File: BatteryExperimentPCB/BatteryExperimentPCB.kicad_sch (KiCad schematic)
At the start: 32 parts, among them J1 USB_C_Receptacle_USB2.0_14P, J2 Conn_01x11_Pin, J3 Conn_01x11_Pin, Q1 DMG1012T, SW1 SW_Push, U1 ATtiny3226-M, U2 USBLC6-2P6, U3 BQ25628RYKR

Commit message: cleanup
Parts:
- D2: footprint (none) -> LED_SMD:LED_0805_2012Metric
- L1: footprint (none) -> Inductor_SMD:L_0805_2012Metric
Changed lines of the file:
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@@
 			)
 		)
-		(property "Footprint" ""
+		(property "Footprint" "Inductor_SMD:L_0805_2012Metric"
 			(at 168.91 55.88 0)
 			(effects
@@
 			)
 		)
-		(property "Footprint" ""
+		(property "Footprint" "LED_SMD:LED_0805_2012Metric"
 			(at 207.01 72.39 0)
 			(effects

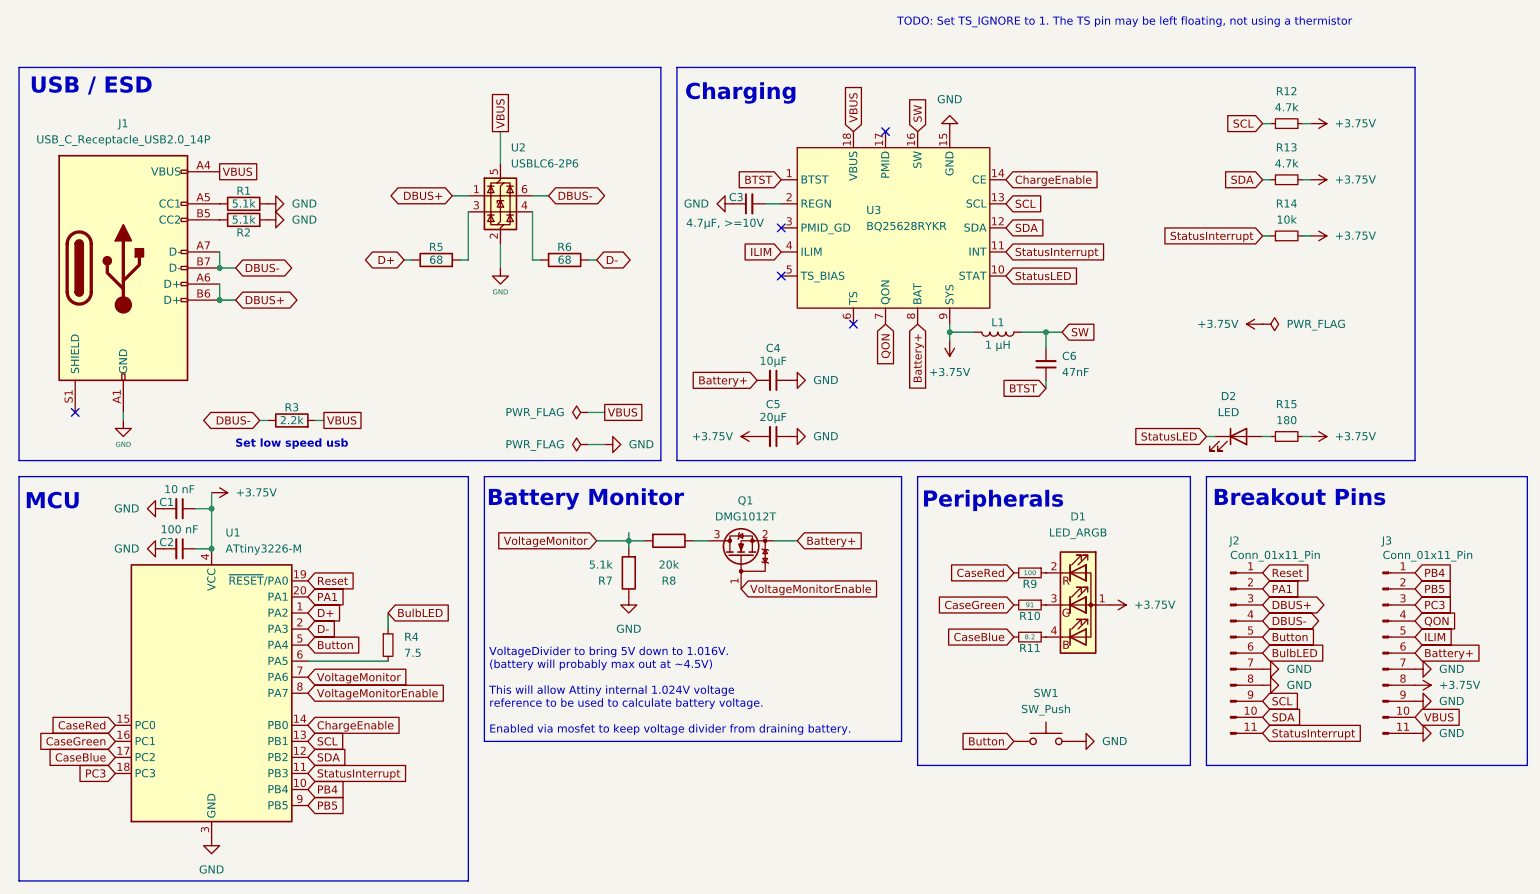
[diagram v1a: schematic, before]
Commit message: add PMID and PMID_GO pins to breakout
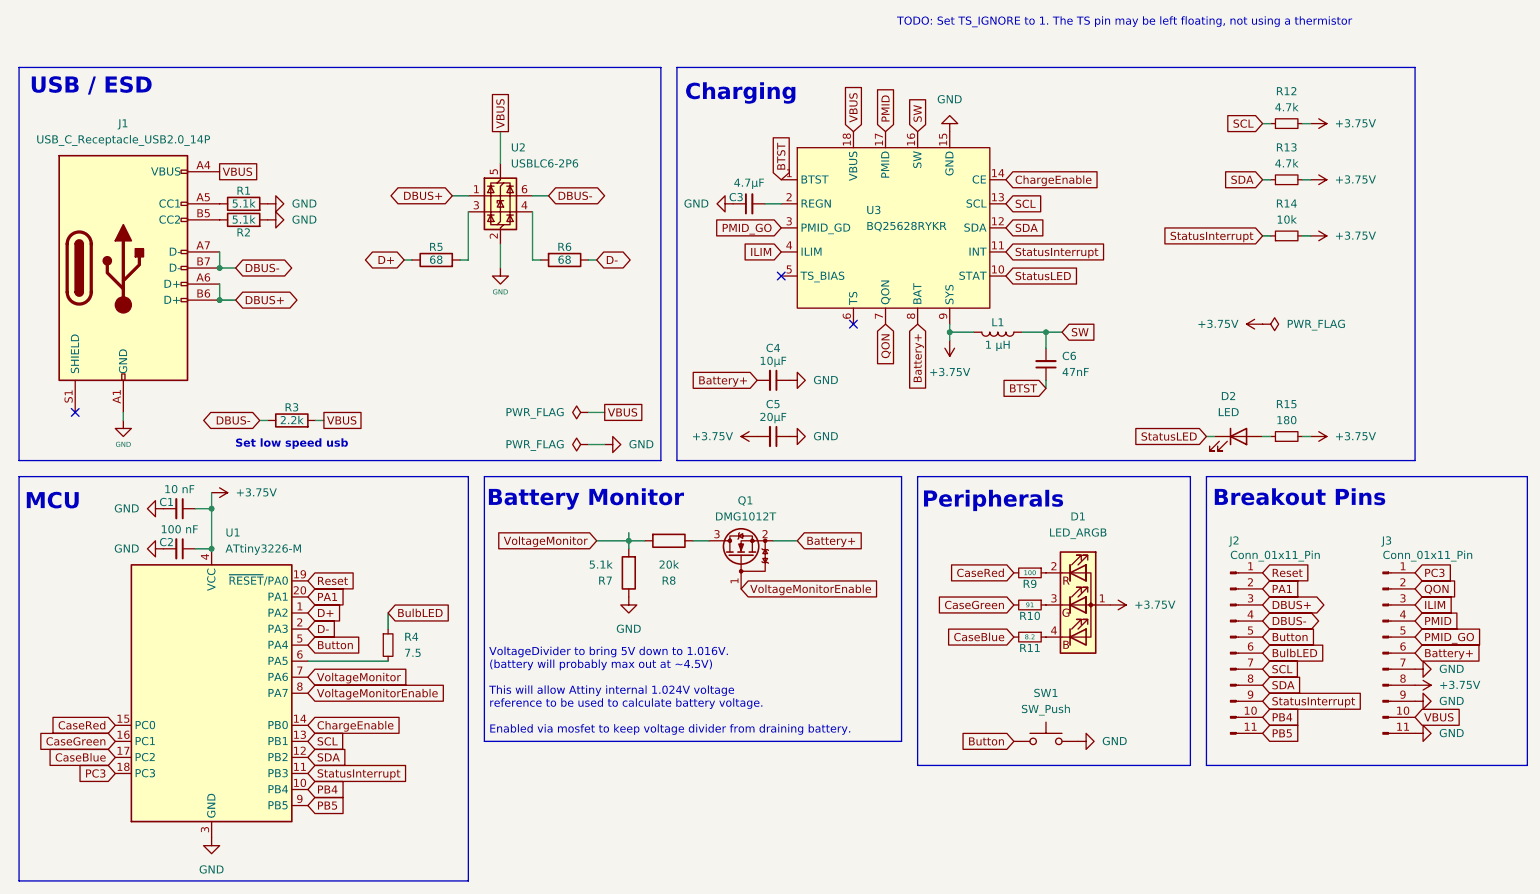
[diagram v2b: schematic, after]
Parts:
- C3: value 4.7μF, >=10V -> 4.7μF
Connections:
- net GND: no longer J2.7 (Pin_7), J2.8 (Pin_8)
- net ILIM: now also J3.3 (Pin_3); no longer J3.5 (Pin_5)
- net PB4: now also J2.10 (Pin_10); no longer J3.1 (Pin_1)
- net PB5: now also J2.11 (Pin_11); no longer J3.2 (Pin_2)
- net PC3: now also J3.1 (Pin_1); no longer J3.3 (Pin_3)
- net QON: now also J3.2 (Pin_2); no longer J3.4 (Pin_4)
- net SCL: now also J2.7 (Pin_7); no longer J2.9 (Pin_9)
- net SDA: now also J2.8 (Pin_8); no longer J2.10 (Pin_10)
- net StatusInterrupt: now also J2.9 (Pin_9); no longer J2.11 (Pin_11)
- net PMID: now reaches U3.17 (PMID)
- net PMID: now also J3.4 (Pin_4)
- net PMID_GO: now reaches U3.3 (PMID_GD)
- net PMID_GO: now also J3.5 (Pin_5)
- no-connect marks 5 -> 3

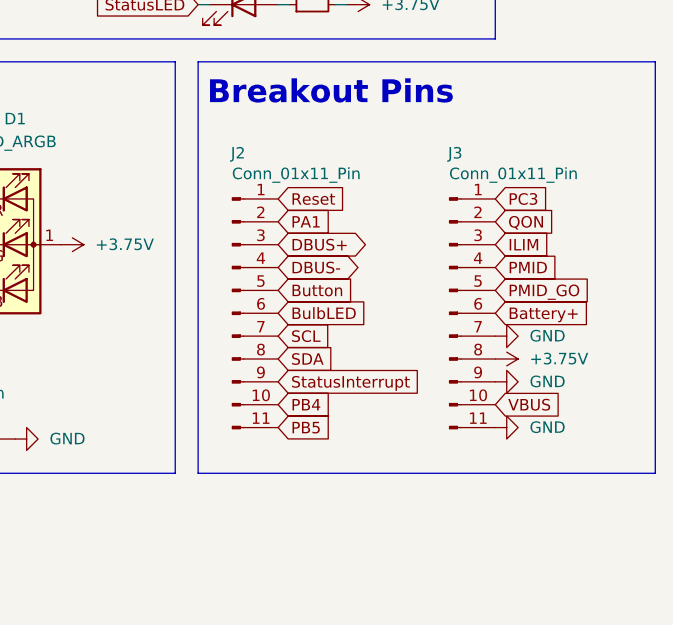
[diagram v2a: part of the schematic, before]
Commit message: added 12th row to breakout, cleanup
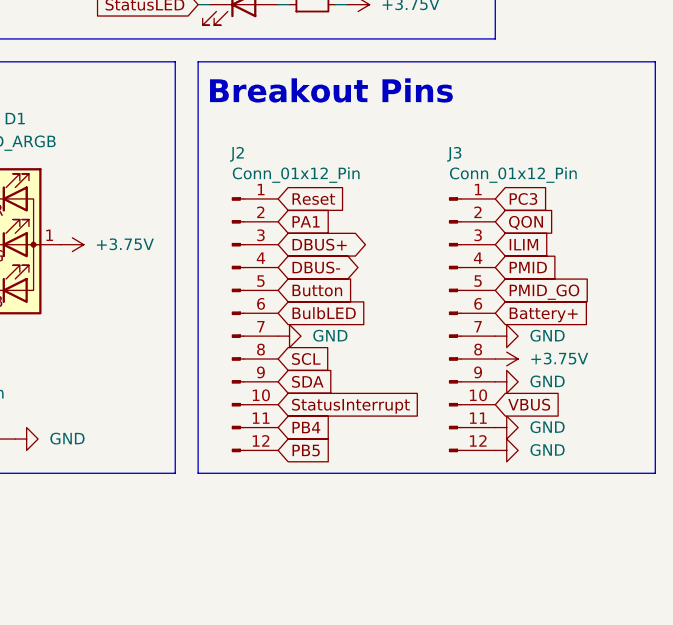
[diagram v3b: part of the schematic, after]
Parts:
- removed J2, J3: Conn_01x11_Pin, Connector_PinHeader_2.54mm:PinHeader_1x11_P2.54mm_Vertical, symbol Connector:Conn_01x11_Pin
- added J2, J3: Conn_01x12_Pin, symbol Connector:Conn_01x12_Pin
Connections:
- net +3.75V: now also J3.8 (Pin_8)
- net Battery+: now also J3.6 (Pin_6)
- net BulbLED: now also J2.6 (Pin_6)
- net Button: now also J2.5 (Pin_5)
- net DBUS+: now also J2.3 (Pin_3)
- net DBUS-: now also J2.4 (Pin_4)
- net GND: now also J2.7 (Pin_7), J3.11 (Pin_11), J3.12 (Pin_12), J3.7 (Pin_7), J3.9 (Pin_9)
- net ILIM: now also J3.3 (Pin_3)
- net PA1: now also J2.2 (Pin_2)
- net PB4: now also J2.11 (Pin_11)
- net PB5: now also J2.12 (Pin_12)
- net PC3: now also J3.1 (Pin_1)
- net PMID: now also J3.4 (Pin_4)
- net PMID_GO: now also J3.5 (Pin_5)
- net QON: now also J3.2 (Pin_2)
- net Reset: now also J2.1 (Pin_1)
- net SCL: now also J2.8 (Pin_8)
- net SDA: now also J2.9 (Pin_9)
- net StatusInterrupt: now also J2.10 (Pin_10)
- net VBUS: now also J3.10 (Pin_10)

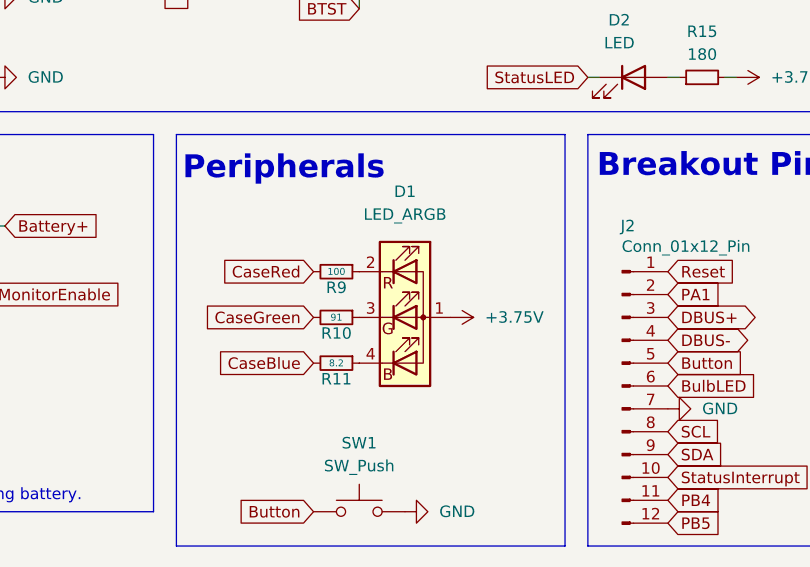
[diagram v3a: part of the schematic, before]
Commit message: copied and customised LED_RBGA symbol for chosen part
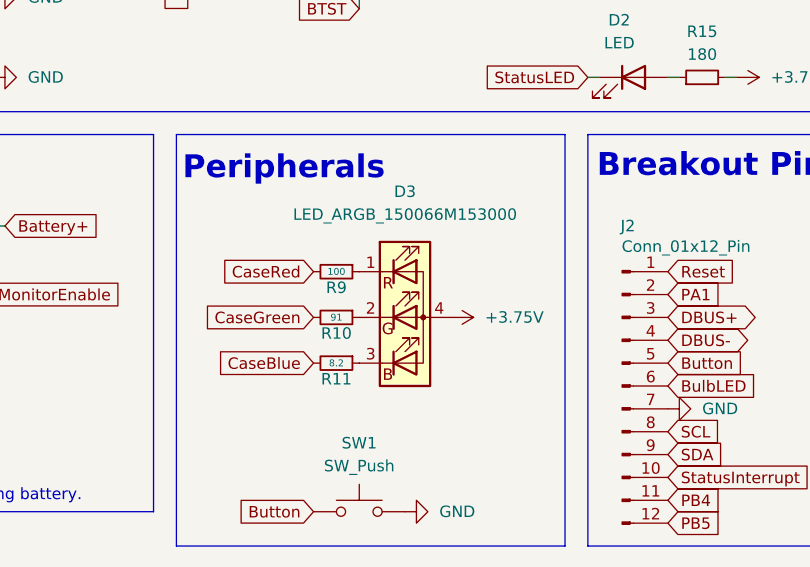
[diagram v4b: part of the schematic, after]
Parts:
- removed D1: LED_ARGB, symbol Device:LED_ARGB
- added D3: LED_ARGB_150066M153000, symbol BatteryExperimentPCB:LED_ARGB_150066M153000
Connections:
- net +3.75V: now also D3.4 (A)
- net at R11.1: now also D3.3 (BK)
- net at R9.1: now also D3.1 (RK)
- net at R10.1: now also D3.2 (GK)
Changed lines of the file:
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@@
-	)
-	(symbol
-		(lib_id "Device:LED_ARGB")
-		(at 181.61 99.06 0)
-		(unit 1)
-		(exclude_from_sim no)
-		(in_bom yes)
-		(on_board yes)
-		(dnp no)
-		(fields_autoplaced yes)
-		(property "Reference" "D1"
-			(at 181.61 85.09 0)
-			(effects
-				(font
-					(size 1.27 1.27)
-				)
-			)
-		)
-		(property "Value" "LED_ARGB"
-			(at 181.61 87.63 0)
-			(effects
-				(font
-					(size 1.27 1.27)
-				)
-			)
-		)
-		(property "Footprint" ""
-			(at 181.61 100.33 0)
-			(effects
-				(font
-					(size 1.27 1.27)
-				)
-				(hide yes)
-			)
-		)
-		(property "Datasheet" "https://www.we-online.com/components/products/datasheet/150066M153000.pdf"
-			(at 181.61 100.33 0)
-			(effects
-				(font
-					(size 1.27 1.27)
-				)
-				(hide yes)
-			)
-		)
-		(property "Description" "RGB LED, anode/red/green/blue"
-			(at 181.61 99.06 0)
-			(effects
-				(font
-					(size 1.27 1.27)
-				)
-				(hide yes)
-			)
-		)
-		(pin "3"
-		)
-		(pin "1"
-		)
-		(pin "4"
-		)
-		(pin "2"
-		)
-		(instances
-			(project ""
-				(path "/057a57c5-fa69-4f68-8ff5-75480ccd2fb3"
-					(reference "D1")
-					(unit 1)
-				)
-			)
-		)
 	)
 	(symbol
@@
 					(unit 1)
 				)
+			)
+		)
+	)
+	(symbol
+		(lib_id "BatteryExperimentPCB:LED_ARGB_150066M153000")
+		(at 181.61 99.06 0)
+		(unit 1)
+		(exclude_from_sim no)
+		(in_bom yes)
+		(on_board yes)
+		(dnp no)
+		(fields_autoplaced yes)
+		(property "Reference" "D3"
+			(at 181.61 85.09 0)
+			(effects
+				(font
+					(size 1.27 1.27)
+				)
+			)
+		)
+		(property "Value" "LED_ARGB_150066M153000"
+			(at 181.61 87.63 0)
+			(effects
+				(font
+					(size 1.27 1.27)
+				)
+			)
+		)
+		(property "Footprint" ""
+			(at 181.61 100.33 0)
+			(effects
+				(font
+					(size 1.27 1.27)
+				)
+				(hide yes)
+			)
+		)
+		(property "Datasheet" "https://www.we-online.com/components/products/datasheet/150066M153000.pdf"
+			(at 181.61 100.33 0)
+			(effects
+				(font
+					(size 1.27 1.27)
+				)
+				(hide yes)
+			)
+		)
+		(property "Description" "RGB LED, anode/red/green/blue"
+			(at 181.61 99.06 0)
+			(effects
+				(font
+					(size 1.27 1.27)
+				)
+				(hide yes)
+			)
+		)
+		(property "mouser" "https://www.mouser.com/ProductDetail/Wurth-Elektronik/150066M153000?qs=5aG0NVq1C4w6V8uSO7dUTg%3D%3D"
+			(at 181.61 99.06 0)
+			(effects
+				(font
+					(size 1.27 1.27)
+				)
+				(hide yes)
+			)
+		)
+		(pin "2"
+		)
+		(pin "3"
+		)
+		(pin "1"
+		)
+		(pin "4"
+		)
+		(instances
+			(project ""
+				(path "/057a57c5-fa69-4f68-8ff5-75480ccd2fb3"
+					(reference "D3")
+					(unit 1)
+				)

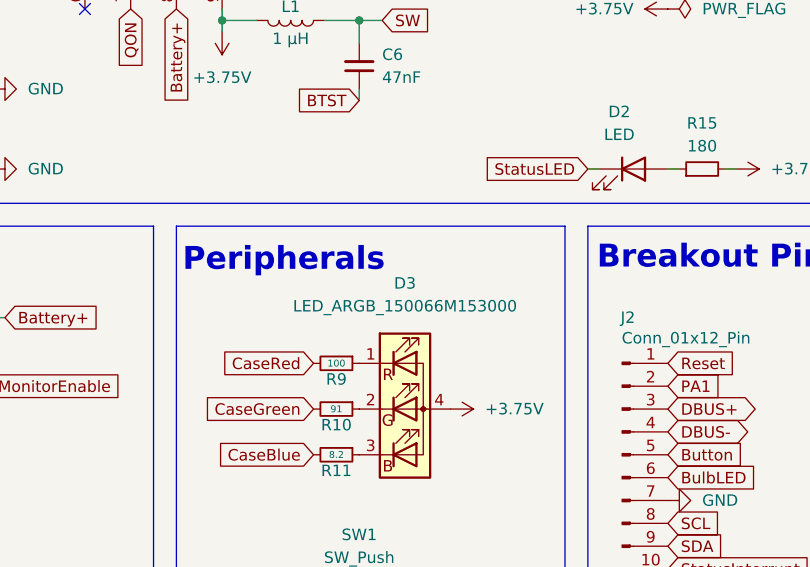
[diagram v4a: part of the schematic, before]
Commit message: added all footprints!
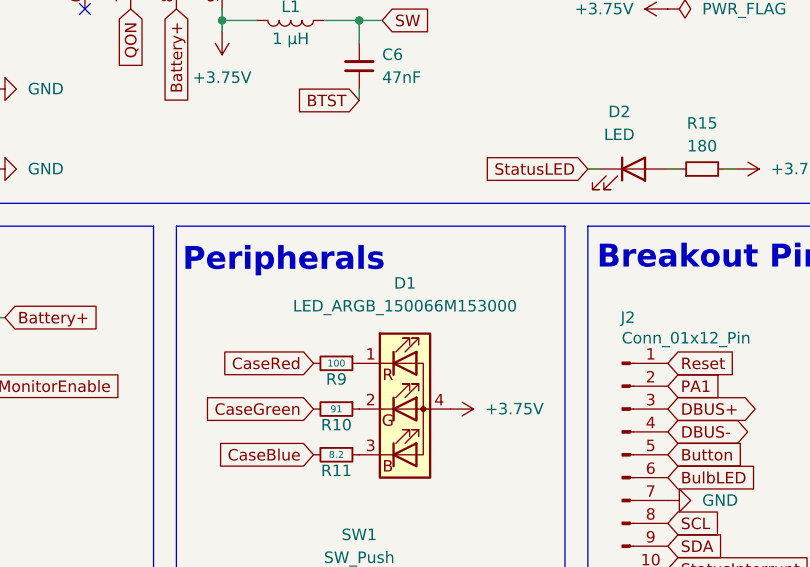
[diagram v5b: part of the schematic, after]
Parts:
- D1: renamed from D3; footprint (none) -> BatteryExperimentPCB:150066M153000
- J2, J3: footprint (none) -> Connector_PinHeader_2.54mm:PinHeader_1x12_P2.54mm_Vertical
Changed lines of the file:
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@@
 			)
 		)
-		(property "Footprint" ""
+		(property "Footprint" "Connector_PinHeader_2.54mm:PinHeader_1x12_P2.54mm_Vertical"
 			(at 205.74 106.68 0)
 			(effects
@@
 			)
 		)
-		(property "Footprint" ""
+		(property "Footprint" "Connector_PinHeader_2.54mm:PinHeader_1x12_P2.54mm_Vertical"
 			(at 229.87 106.68 0)
 			(effects
@@
 		(dnp no)
 		(fields_autoplaced yes)
-		(property "Reference" "D3"
+		(property "Reference" "D1"
 			(at 181.61 85.09 0)
 			(effects
@@
 			)
 		)
-		(property "Footprint" ""
+		(property "Footprint" "BatteryExperimentPCB:150066M153000"
 			(at 181.61 100.33 0)
 			(effects
@@
 			(project ""
 				(path "/057a57c5-fa69-4f68-8ff5-75480ccd2fb3"
-					(reference "D3")
-					(unit 1)
-				)
+					(reference "D1")
+					(unit 1)
+				)

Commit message: actually added all footprints
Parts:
- U3: footprint Resistor_SMD:R_0805_2012Metric -> BatteryExperimentPCB:RYK0018A-MFG
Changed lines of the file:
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@@
 			)
 		)
-		(property "Footprint" "Resistor_SMD:R_0805_2012Metric"
+		(property "Footprint" "BatteryExperimentPCB:RYK0018A-MFG"
 			(at 143.51 26.67 0)
 			(effects
@@
 			)
 		)
-		(property "Datasheet" ""
+		(property "Datasheet" "https://www.ti.com/lit/ds/symlink/bq25628.pdf"
 			(at 143.51 26.67 0)
 			(effects
